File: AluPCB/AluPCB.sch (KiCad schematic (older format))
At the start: 19 parts, among them J1 CON_U, J2 CON_U, J3 CON_U, Q1 nfet, Q2 nfet, Q3 nfet, Q4 nfet, Q5 nfet, Q6 nfet

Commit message: aluPCB V1
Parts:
- removed Q1, Q2, Q3, Q4, Q5, Q6: nfet, Package_SON:VSONP-8-1EP_5x6_P1.27mm, symbol Device:Q_NMOS_GDS
- added C1, C10, C11, C12, C13, C14, C15, C16, C17, C18, C19, C2, C20, C21, C22, C23, C24, C25, C26, C27, C28, C29, C3, C30, C31, C32, C33, C34, C35, C36, C37, C38, C39, C4, C40, C41, C42, C43, C44, C45, C46, C47, C48, C49, C5, C50, C51, C52, C53, C54, C55, C56, C57, C58, C59, C6, C60, C7, C8, C9: 2u2, Capacitor_SMD:C_1206_3216Metric, symbol Device:C_Small
- added H1, H2: MountingHole_Pad, MountingHole:MountingHole_4.3mm_M4_DIN965_Pad, symbol Mechanical:MountingHole_Pad
- added Q1, Q2, Q3, Q4, Q5, Q6: AON6276, Package_SON:VSONP-8-1EP_5x6_P1.27mm, symbol Device:Q_NMOS_SGD
- J1, J2, J3: footprint Connector_PinHeader_2.00mm:PinHeader_1x06_P2.00mm_Vertical_SMD_Pin1Right -> Connector_PinSocket_2.00mm:PinSocket_1x06_P2.00mm_Vertical_SMD_Pin1Left
- TH1: renamed from TH?; footprint (none) -> Resistor_SMD:R_0603_1608Metric
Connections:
- net GND: now also C1.2, C10.2, C11.2, C12.2, C13.2, C14.2, C15.2, C16.2, C17.2, C18.2, C19.2, C2.2, C20.2, C21.2, C22.2, C23.2, C24.2, C25.2, C26.2, C27.2, C28.2, C29.2, C3.2, C30.2, C31.2, C32.2, C33.2, C34.2, C35.2, C36.2, C37.2, C38.2, C39.2, C4.2, C40.2, C41.2, C42.2, C43.2, C44.2, C45.2, C46.2, C47.2, C48.2, C49.2, C5.2, C50.2, C51.2, C52.2, C53.2, C54.2, C55.2, C56.2, C57.2, C58.2, C59.2, C6.2, C60.2, C7.2, C8.2, C9.2, H1.1, H2.1; no longer TH1.1
- net GUH: now also Q1.2 (G)
- net GUL: now also Q2.2 (G)
- net GVH: now also Q3.2 (G)
- net GVL: now also Q4.2 (G)
- net GWH: now also Q5.2 (G)
- net GWL: now also Q6.2 (G)
- net IUH: now also J1.4 (Pin_4); no longer J1.5 (Pin_5)
- net IVH: now also J2.4 (Pin_4); no longer J2.5 (Pin_5)
- net IWH: now also J3.4 (Pin_4); no longer J3.5 (Pin_5)
- net U: now also Q1.1 (S), Q2.3 (D)
- net V: now also Q3.1 (S), Q4.3 (D)
- net W: now also Q5.1 (S), Q6.3 (D)
- net at R1.1, R2.2: now also Q2.1 (S)
- net at TH1.2: now also J2.5 (Pin_5); no longer J2.4 (Pin_4)
- net at R4.1, R5.2: now also Q4.1 (S)
- net at R7.1, R8.2: now also Q6.1 (S)
- new net: J3.5 (Pin_5), TH1.1
- new net VIN: C1.1, C10.1, C11.1, C12.1, C13.1, C14.1, C15.1, C16.1, C17.1, C18.1, C19.1, C2.1, C20.1, C21.1, C22.1, C23.1, C24.1, C25.1, C26.1, C27.1, C28.1, C29.1, C3.1, C30.1, C31.1, C32.1, C33.1, C34.1, C35.1, C36.1, C37.1, C38.1, C39.1, C4.1, C40.1, C41.1, C42.1, C43.1, C44.1, C45.1, C46.1, C47.1, C48.1, C49.1, C5.1, C50.1, C51.1, C52.1, C53.1, C54.1, C55.1, C56.1, C57.1, C58.1, C59.1, C6.1, C60.1, C7.1, C8.1, C9.1, Q1.3 (D), Q3.3 (D), Q5.3 (D)
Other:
- moved on the sheet: J3, TH1

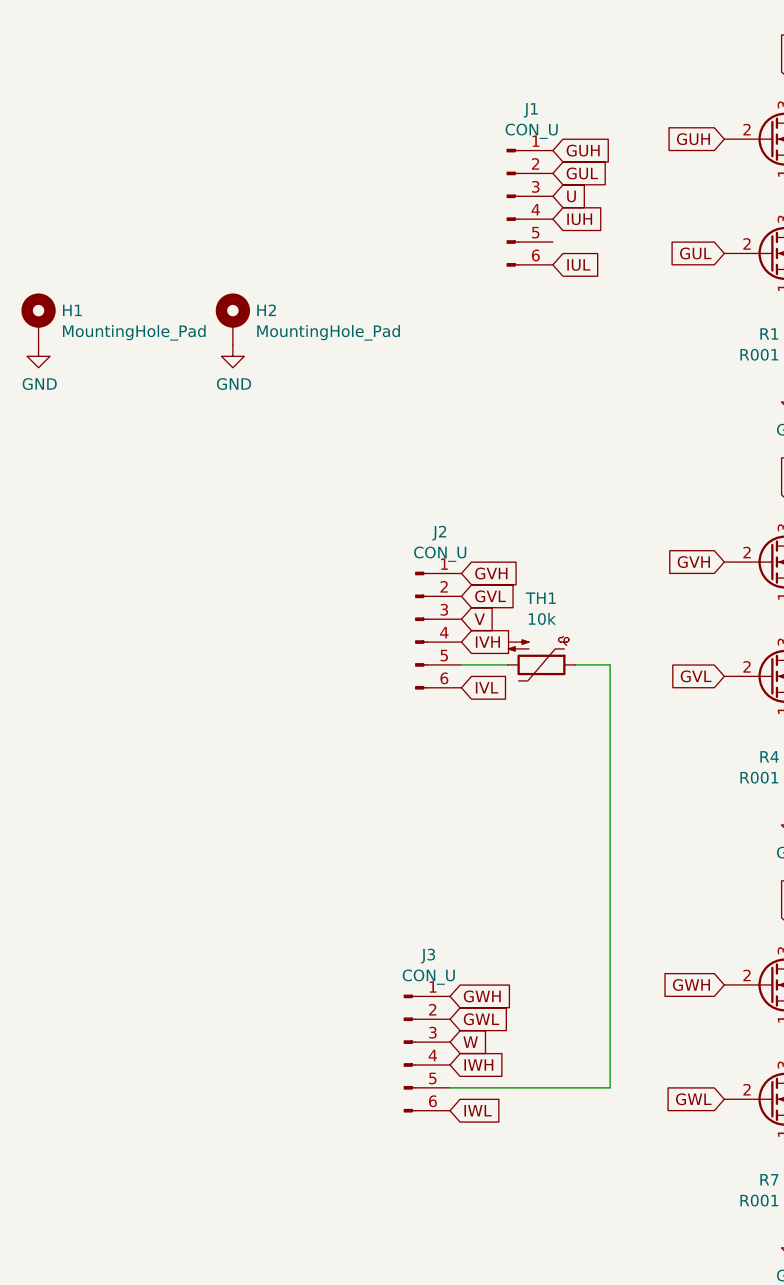
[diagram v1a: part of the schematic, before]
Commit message: finished AluPCB Power Stage 1, added images
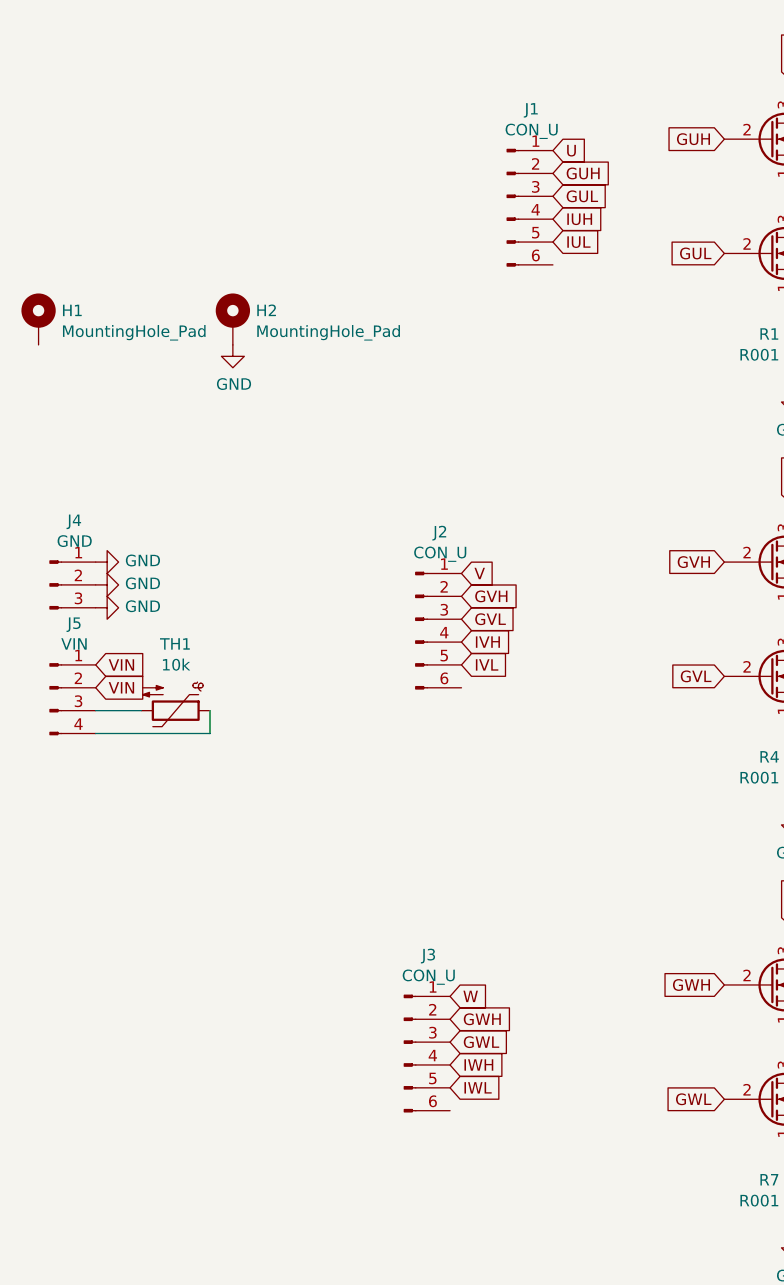
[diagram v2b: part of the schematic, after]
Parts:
- added J4: GND, Connector_PinSocket_2.00mm:PinSocket_1x03_P2.00mm_Vertical_SMD_Pin1Left, symbol Connector:Conn_01x03_Male
- added J5: VIN, Connector_PinSocket_2.00mm:PinSocket_1x04_P2.00mm_Vertical_SMD_Pin1Left, symbol Connector:Conn_01x04_Male
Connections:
- net GND: now also J4.1 (Pin_1), J4.2 (Pin_2), J4.3 (Pin_3); no longer H1.1
- net GUH: now also J1.2 (Pin_2); no longer J1.1 (Pin_1)
- net GUL: now also J1.3 (Pin_3); no longer J1.2 (Pin_2)
- net GVH: now also J2.2 (Pin_2); no longer J2.1 (Pin_1)
- net GVL: now also J2.3 (Pin_3); no longer J2.2 (Pin_2)
- net GWH: now also J3.2 (Pin_2); no longer J3.1 (Pin_1)
- net GWL: now also J3.3 (Pin_3); no longer J3.2 (Pin_2)
- net IUL: now also J1.5 (Pin_5); no longer J1.6 (Pin_6)
- net IVL: now also J2.5 (Pin_5); no longer J2.6 (Pin_6)
- net IWL: now also J3.5 (Pin_5); no longer J3.6 (Pin_6)
- net U: now also J1.1 (Pin_1); no longer J1.3 (Pin_3)
- net V: now also J2.1 (Pin_1); no longer J2.3 (Pin_3)
- net VIN: now also J5.1 (Pin_1), J5.2 (Pin_2)
- net W: now also J3.1 (Pin_1); no longer J3.3 (Pin_3)
- net at TH1.1: now also J5.4 (Pin_4); no longer J3.5 (Pin_5)
- net at TH1.2: now also J5.3 (Pin_3); no longer J2.5 (Pin_5)
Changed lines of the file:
@@
 	1    0    0    -1
 $EndComp
+Text GLabel 2950 1400 2    50   Input ~ 0
+GUH
+Text GLabel 2950 1500 2    50   Input ~ 0
+GUL
 Text GLabel 2950 1300 2    50   Input ~ 0
-GUH
-Text GLabel 2950 1400 2    50   Input ~ 0
-GUL
-Text GLabel 2950 1500 2    50   Input ~ 0
 U
 Text GLabel 2950 1600 2    50   Input ~ 0
 IUH
-Text GLabel 2950 1800 2    50   Input ~ 0
+Text GLabel 2950 1700 2    50   Input ~ 0
 IUL
 $Comp
@@
 	1    0    0    -1
 $EndComp
+Text GLabel 2550 3250 2    50   Input ~ 0
+GVH
+Text GLabel 2550 3350 2    50   Input ~ 0
+GVL
 Text GLabel 2550 3150 2    50   Input ~ 0
-GVH
-Text GLabel 2550 3250 2    50   Input ~ 0
-GVL
-Text GLabel 2550 3350 2    50   Input ~ 0
 V
 Text GLabel 2550 3450 2    50   Input ~ 0
 IVH
-Text GLabel 2550 3650 2    50   Input ~ 0
+Text GLabel 2550 3550 2    50   Input ~ 0
 IVL
 $Comp
@@
 	1    0    0    -1
 $EndComp
+Text GLabel 2500 5100 2    50   Input ~ 0
+GWH
+Text GLabel 2500 5200 2    50   Input ~ 0
+GWL
 Text GLabel 2500 5000 2    50   Input ~ 0
-GWH
-Text GLabel 2500 5100 2    50   Input ~ 0
-GWL
-Text GLabel 2500 5200 2    50   Input ~ 0
 W
 Text GLabel 2500 5300 2    50   Input ~ 0
 IWH
-Text GLabel 2500 5500 2    50   Input ~ 0
+Text GLabel 2500 5400 2    50   Input ~ 0
 IWL
-$Comp
-L Device:Thermistor_NTC TH1
-U 1 1 5CC4C81B
-P 2900 3550
-F 0 "TH1" V 2610 3550 50  0000 C CNN
-F 1 "10k" V 2701 3550 50  0000 C CNN
-F 2 "Resistor_SMD:R_0603_1608Metric" H 2900 3600 50  0001 C CNN
-F 3 "~" H 2900 3600 50  0001 C CNN
-	1    2900 3550
-	0    1    1    0
-$EndComp
-Wire Wire Line
-	2750 3550 2550 3550
-Wire Wire Line
-	3200 3550 3050 3550
 $Comp
 L Device:Q_NMOS_SGD Q1
@@
 	1    0    0    -1
 $EndComp
-Wire Wire Line
-	3200 5400 3200 3550
-Wire Wire Line
-	2500 5400 3200 5400
 $Comp
 L Mechanical:MountingHole_Pad H2
@@
 $EndComp
 $Comp
-L power:GND #PWR0104
-U 1 1 5CC8BD6B
-P 700 2150
-F 0 "#PWR0104" H 700 1900 50  0001 C CNN
-F 1 "GND" H 705 1977 50  0000 C CNN
-F 2 "" H 700 2150 50  0001 C CNN
-F 3 "" H 700 2150 50  0001 C CNN
-	1    700  2150
-	1    0    0    -1
-$EndComp
-$Comp
 L power:GND #PWR0105
 U 1 1 5CC8C189
@@
 Text GLabel 7950 4550 1    50   Input ~ 0
 VIN
+$Comp
+L Device:Thermistor_NTC TH1
+U 1 1 5CDFE2AF
+P 1300 3750
+F 0 "TH1" V 1010 3750 50  0000 C CNN
+F 1 "10k" V 1101 3750 50  0000 C CNN
+F 2 "Resistor_SMD:R_0603_1608Metric" H 1300 3800 50  0001 C CNN
+F 3 "~" H 1300 3800 50  0001 C CNN
+	1    1300 3750
+	0    1    1    0
+$EndComp
+Wire Wire Line
+	1150 3750 950  3750
+Wire Wire Line
+	1450 3750 1450 3850
+Wire Wire Line
+	1450 3850 950  3850
+$Comp
+L power:GND #PWR0166
+U 1 1 5CE018CC
+P 950 3100
+F 0 "#PWR0166" H 950 2850 50  0001 C CNN
+F 1 "GND" V 955 2972 50  0000 R CNN
+F 2 "" H 950 3100 50  0001 C CNN
+F 3 "" H 950 3100 50  0001 C CNN
+	1    950  3100
+	0    -1   -1   0
+$EndComp
+$Comp
+L power:GND #PWR0167
+U 1 1 5CE0266F
+P 950 3200
+F 0 "#PWR0167" H 950 2950 50  0001 C CNN
+F 1 "GND" V 955 3072 50  0000 R CNN
+F 2 "" H 950 3200 50  0001 C CNN
+F 3 "" H 950 3200 50  0001 C CNN
+	1    950  3200
+	0    -1   -1   0
+$EndComp
+Text GLabel 950  3550 2    50   Input ~ 0
+VIN
+Text GLabel 950  3650 2    50   Input ~ 0
+VIN
+$Comp
+L Connector:Conn_01x03_Male J4
+U 1 1 5CE7A930
+P 750 3200
+F 0 "J4" H 858 3481 50  0000 C CNN
+F 1 "GND" H 858 3390 50  0000 C CNN
+F 2 "Connector_PinSocket_2.00mm:PinSocket_1x03_P2.00mm_Vertical_SMD_Pin1Left" H 750 3200 50  0001 C CNN
+F 3 "~" H 750 3200 50  0001 C CNN
+	1    750  3200
+	1    0    0    -1
+$EndComp
+$Comp
+L Connector:Conn_01x04_Male J5
+U 1 1 5CE7B946
+P 750 3650
+F 0 "J5" H 858 3931 50  0000 C CNN
+F 1 "VIN" H 858 3840 50  0000 C CNN
+F 2 "Connector_PinSocket_2.00mm:PinSocket_1x04_P2.00mm_Vertical_SMD_Pin1Left" H 750 3650 50  0001 C CNN
+F 3 "~" H 750 3650 50  0001 C CNN
+	1    750  3650
+	1    0    0    -1
+$EndComp
+$Comp
+L power:GND #PWR0168
+U 1 1 5CE7D54B
+P 950 3300
+F 0 "#PWR0168" H 950 3050 50  0001 C CNN
+F 1 "GND" V 955 3172 50  0000 R CNN
+F 2 "" H 950 3300 50  0001 C CNN
+F 3 "" H 950 3300 50  0001 C CNN
+	1    950  3300
+	0    -1   -1   0
+$EndComp
 $EndSCHEMATC

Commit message: wip
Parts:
- removed J5: VIN, Connector_PinSocket_2.00mm:PinSocket_1x04_P2.00mm_Vertical_SMD_Pin1Left, symbol Connector:Conn_01x04_Male
- added J5: VIN, Connector_PinSocket_2.00mm:PinSocket_1x03_P2.00mm_Vertical_SMD_Pin1Left, symbol Connector:Conn_01x03_Male
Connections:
- net VIN: now also J5.3 (Pin_3)
- net at TH1.1: now also J5.2 (Pin_2)
- net at TH1.2: now also J5.1 (Pin_1)
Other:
- moved on the sheet: TH1
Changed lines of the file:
@@
 L Device:Thermistor_NTC TH1
 U 1 1 5CDFE2AF
-P 1300 3750
-F 0 "TH1" V 1010 3750 50  0000 C CNN
-F 1 "10k" V 1101 3750 50  0000 C CNN
-F 2 "Resistor_SMD:R_0603_1608Metric" H 1300 3800 50  0001 C CNN
-F 3 "~" H 1300 3800 50  0001 C CNN
-	1    1300 3750
+P 1300 3650
+F 0 "TH1" V 1010 3650 50  0000 C CNN
+F 1 "10k" V 1101 3650 50  0000 C CNN
+F 2 "Resistor_SMD:R_0603_1608Metric" H 1300 3700 50  0001 C CNN
+F 3 "~" H 1300 3700 50  0001 C CNN
+	1    1300 3650
 	0    1    1    0
 $EndComp
 Wire Wire Line
-	1150 3750 950  3750
+	1150 3650 950  3650
 Wire Wire Line
-	1450 3750 1450 3850
+	1450 3650 1450 3750
 Wire Wire Line
-	1450 3850 950  3850
+	1450 3750 950  3750
 $Comp
 L power:GND #PWR0166
@@
 	0    -1   -1   0
 $EndComp
-Text GLabel 950  3550 2    50   Input ~ 0
-VIN
-Text GLabel 950  3650 2    50   Input ~ 0
+Text GLabel 950  3850 2    50   Input ~ 0
 VIN
 $Comp
@@
 $EndComp
 $Comp
-L Connector:Conn_01x04_Male J5
-U 1 1 5CE7B946
-P 750 3650
-F 0 "J5" H 858 3931 50  0000 C CNN
-F 1 "VIN" H 858 3840 50  0000 C CNN
-F 2 "Connector_PinSocket_2.00mm:PinSocket_1x04_P2.00mm_Vertical_SMD_Pin1Left" H 750 3650 50  0001 C CNN
-F 3 "~" H 750 3650 50  0001 C CNN
-	1    750  3650
-	1    0    0    -1
-$EndComp
-$Comp
 L power:GND #PWR0168
 U 1 1 5CE7D54B
@@
 	0    -1   -1   0
 $EndComp
+$Comp
+L Connector:Conn_01x03_Male J5
+U 1 1 5CCA217B
+P 750 3750
+F 0 "J5" H 858 4031 50  0000 C CNN
+F 1 "VIN" H 858 3940 50  0000 C CNN
+F 2 "Connector_PinSocket_2.00mm:PinSocket_1x03_P2.00mm_Vertical_SMD_Pin1Left" H 750 3750 50  0001 C CNN
+F 3 "~" H 750 3750 50  0001 C CNN
+	1    750  3750
+	1    0    0    -1
+$EndComp
 $EndSCHEMATC
